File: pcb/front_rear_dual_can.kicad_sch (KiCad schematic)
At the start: 0 parts

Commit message: Configured hierarchical sheets and added CAN sheet.
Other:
- added sheet Cockpit (cockpit.kicad_sch)
- added sheet Front Zone (front_zone.kicad_sch)
- added sheet Power (power.kicad_sch)
- added sheet Rear Zone (rear_zone.kicad_sch)
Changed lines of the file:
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@@
 	(generator_version "10.0")
 	(paper "A4")
+	(sheet
+		(at 123.19 80.01)
+		(size 43.18 43.18)
+		(exclude_from_sim no)
+		(in_bom yes)
+		(on_board yes)
+		(dnp no)
+		(fields_autoplaced yes)
+		(stroke
+			(width 0.1524)
+			(type solid)
+		)
+		(fill
+			(color 0 0 0 0)
+		)
+		(property "Sheetname" "Power"
+			(at 123.19 79.2984 0)
+			(show_name no)
+			(do_not_autoplace no)
+			(effects
+				(font
+					(size 1.27 1.27)
+				)
+				(justify left bottom)
+			)
+		)
+		(property "Sheetfile" "power.kicad_sch"
+			(at 123.19 123.7746 0)
+			(show_name no)
+			(do_not_autoplace no)
+			(effects
+				(font
+					(size 1.27 1.27)
+				)
+				(justify left top)
+			)
+		)
+		(instances
+			(project "front_rear_dual_can"
+				(path "/11f1b6cb-7ca3-4657-a79b-c672c999e35e"
+					(page "5")
+				)
+			)
+		)
+	)
+	(sheet
+		(at 120.65 29.21)
+		(size 24.13 12.7)
+		(exclude_from_sim no)
+		(in_bom yes)
+		(on_board yes)
+		(dnp no)
+		(fields_autoplaced yes)
+		(stroke
+			(width 0.1524)
+			(type solid)
+		)
+		(fill
+			(color 0 0 0 0)
+		)
+		(property "Sheetname" "Cockpit"
+			(at 120.65 28.4984 0)
+			(show_name no)
+			(do_not_autoplace no)
+			(effects
+				(font
+					(size 1.27 1.27)
+				)
+				(justify left bottom)
+			)
+		)
+		(property "Sheetfile" "cockpit.kicad_sch"
+			(at 120.65 42.4946 0)
+			(show_name no)
+			(do_not_autoplace no)
+			(effects
+				(font
+					(size 1.27 1.27)
+				)
+				(justify left top)
+			)
+		)
+		(instances
+			(project "front_rear_dual_can"
+				(path "/11f1b6cb-7ca3-4657-a79b-c672c999e35e"
+					(page "4")
+				)
+			)
+		)
+	)
+	(sheet
+		(at 187.96 91.44)
+		(size 35.56 35.56)
+		(exclude_from_sim no)
+		(in_bom yes)
+		(on_board yes)
+		(dnp no)
+		(fields_autoplaced yes)
+		(stroke
+			(width 0.1524)
+			(type solid)
+		)
+		(fill
+			(color 0 0 0 0)
+		)
+		(property "Sheetname" "Front Zone"
+			(at 187.96 90.7284 0)
+			(show_name no)
+			(do_not_autoplace no)
+			(effects
+				(font
+					(size 1.27 1.27)
+				)
+				(justify left bottom)
+			)
+		)
+		(property "Sheetfile" "front_zone.kicad_sch"
+			(at 187.96 127.5846 0)
+			(show_name no)
+			(do_not_autoplace no)
+			(effects
+				(font
+					(size 1.27 1.27)
+				)
+				(justify left top)
+			)
+		)
+		(instances
+			(project "front_rear_dual_can"
+				(path "/11f1b6cb-7ca3-4657-a79b-c672c999e35e"
+					(page "2")
+				)
+			)
+		)
+	)
+	(sheet
+		(at 107.95 166.37)
+		(size 30.48 17.78)
+		(exclude_from_sim no)
+		(in_bom yes)
+		(on_board yes)
+		(dnp no)
+		(fields_autoplaced yes)
+		(stroke
+			(width 0.1524)
+			(type solid)
+		)
+		(fill
+			(color 0 0 0 0)
+		)
+		(property "Sheetname" "Rear Zone"
+			(at 107.95 165.6584 0)
+			(show_name no)
+			(do_not_autoplace no)
+			(effects
+				(font
+					(size 1.27 1.27)
+				)
+				(justify left bottom)
+			)
+		)
+		(property "Sheetfile" "rear_zone.kicad_sch"
+			(at 107.95 184.7346 0)
+			(show_name no)
+			(do_not_autoplace no)
+			(effects
+				(font
+					(size 1.27 1.27)
+				)
+				(justify left top)
+			)
+		)
+		(instances
+			(project "front_rear_dual_can"
+				(path "/11f1b6cb-7ca3-4657-a79b-c672c999e35e"
+					(page "3")
+				)
+			)
+		)
+	)
 	(sheet_instances
 		(path "/"

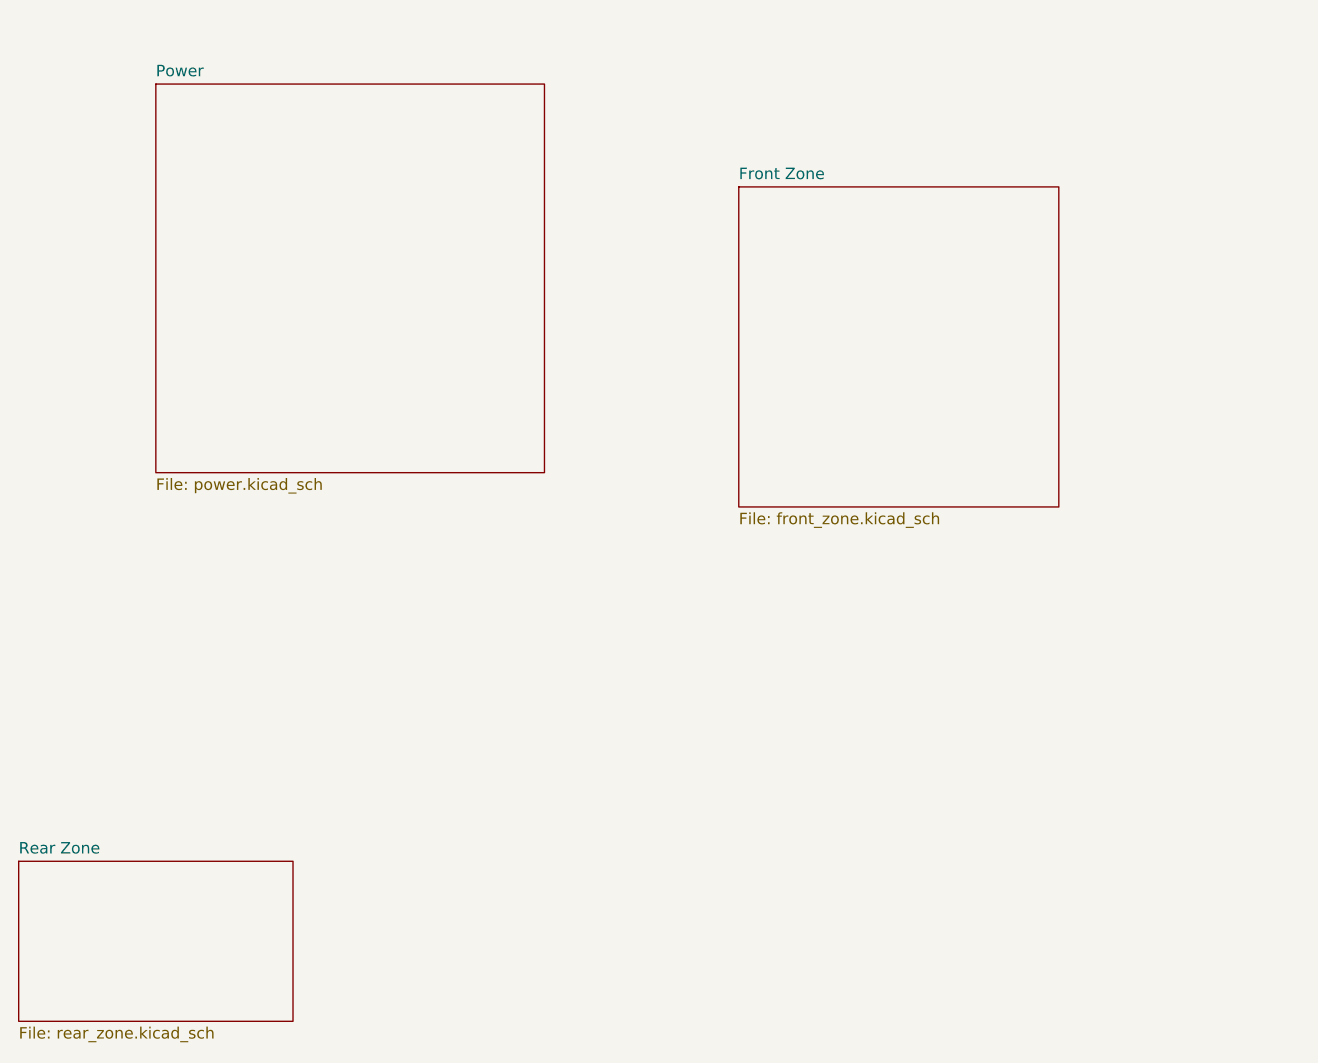
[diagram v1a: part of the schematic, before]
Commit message: Added Front and Rear zone sheets made of CAN and MCU design sheets.
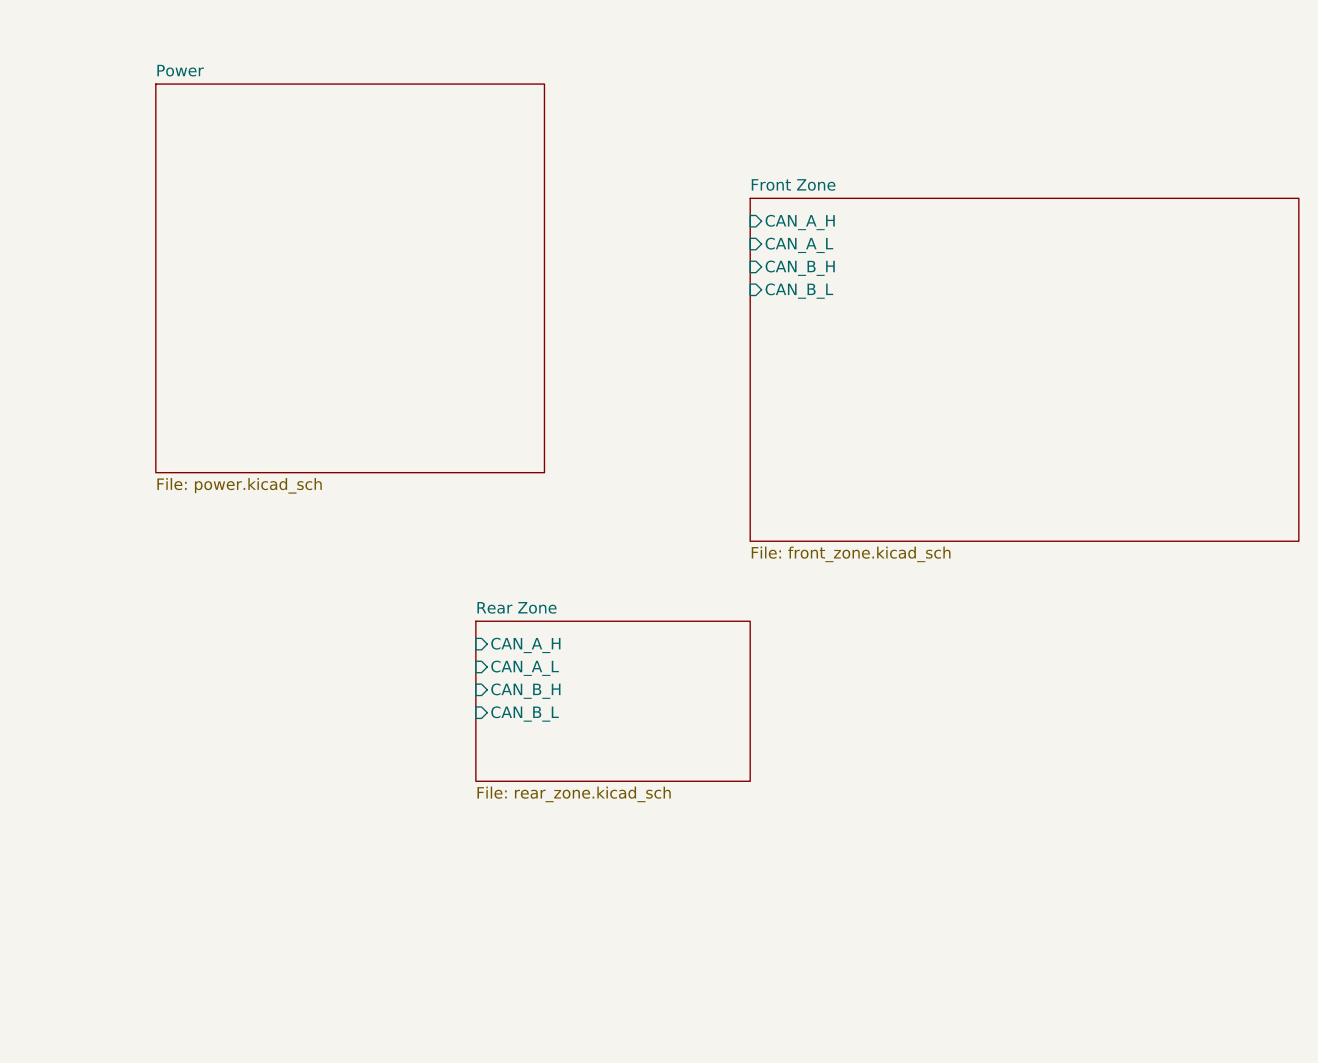
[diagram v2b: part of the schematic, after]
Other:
- sheet Front Zone ports: added CAN_A_H, CAN_A_L, CAN_B_H, CAN_B_L; removed none
- sheet Rear Zone ports: added CAN_A_H, CAN_A_L, CAN_B_H, CAN_B_L; removed none
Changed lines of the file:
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@@
 	)
 	(sheet
-		(at 187.96 91.44)
-		(size 35.56 35.56)
+		(at 189.23 92.71)
+		(size 60.96 38.1)
 		(exclude_from_sim no)
 		(in_bom yes)
@@
 		)
 		(property "Sheetname" "Front Zone"
-			(at 187.96 90.7284 0)
+			(at 189.23 91.9984 0)
 			(show_name no)
 			(do_not_autoplace no)
@@
 		)
 		(property "Sheetfile" "front_zone.kicad_sch"
-			(at 187.96 127.5846 0)
+			(at 189.23 131.3946 0)
 			(show_name no)
 			(do_not_autoplace no)
@@
 				)
 				(justify left top)
+			)
+		)
+		(pin "CAN_A_H" input
+			(at 189.23 95.25 180)
+			(effects
+				(font
+					(size 1.27 1.27)
+				)
+				(justify left)
+			)
+		)
+		(pin "CAN_A_L" input
+			(at 189.23 97.79 180)
+			(effects
+				(font
+					(size 1.27 1.27)
+				)
+				(justify left)
+			)
+		)
+		(pin "CAN_B_H" input
+			(at 189.23 100.33 180)
+			(effects
+				(font
+					(size 1.27 1.27)
+				)
+				(justify left)
+			)
+		)
+		(pin "CAN_B_L" input
+			(at 189.23 102.87 180)
+			(effects
+				(font
+					(size 1.27 1.27)
+				)
+				(justify left)
 			)
 		)
@@
 	)
 	(sheet
-		(at 107.95 166.37)
+		(at 158.75 139.7)
 		(size 30.48 17.78)
 		(exclude_from_sim no)
@@
 		)
 		(property "Sheetname" "Rear Zone"
-			(at 107.95 165.6584 0)
+			(at 158.75 138.9884 0)
 			(show_name no)
 			(do_not_autoplace no)
@@
 		)
 		(property "Sheetfile" "rear_zone.kicad_sch"
-			(at 107.95 184.7346 0)
+			(at 158.75 158.0646 0)
 			(show_name no)
 			(do_not_autoplace no)
@@
 			)
 		)
+		(pin "CAN_A_H" input
+			(at 158.75 142.24 180)
+			(effects
+				(font
+					(size 1.27 1.27)
+				)
+				(justify left)
+			)
+		)
+		(pin "CAN_A_L" input
+			(at 158.75 144.78 180)
+			(effects
+				(font
+					(size 1.27 1.27)
+				)
+				(justify left)
+			)
+		)
+		(pin "CAN_B_H" input
+			(at 158.75 147.32 180)
+			(effects
+				(font
+					(size 1.27 1.27)
+				)
+				(justify left)
+			)
+		)
+		(pin "CAN_B_L" input
+			(at 158.75 149.86 180)
+			(effects
+				(font
+					(size 1.27 1.27)
+				)
+				(justify left)
+			)
+		)

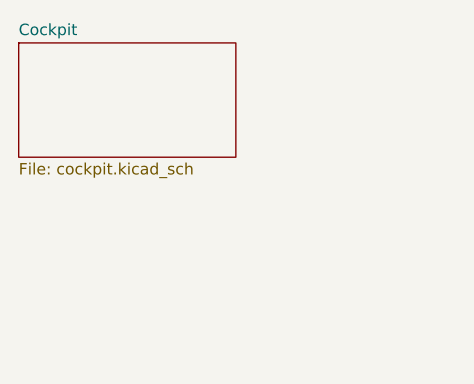
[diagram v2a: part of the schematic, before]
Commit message: Added Cockpit and Power sheets.
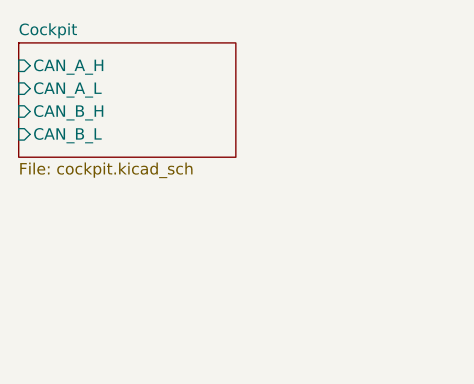
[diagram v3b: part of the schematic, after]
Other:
- sheet Cockpit ports: added CAN_A_H, CAN_A_L, CAN_B_H, CAN_B_L; removed none
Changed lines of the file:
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@@
+			)
+		)
+		(pin "CAN_A_H" input
+			(at 120.65 31.75 180)
+			(effects
+				(font
+					(size 1.27 1.27)
+				)
+				(justify left)
+			)
+		)
+		(pin "CAN_A_L" input
+			(at 120.65 34.29 180)
+			(effects
+				(font
+					(size 1.27 1.27)
+				)
+				(justify left)
+			)
+		)
+		(pin "CAN_B_H" input
+			(at 120.65 36.83 180)
+			(effects
+				(font
+					(size 1.27 1.27)
+				)
+				(justify left)
+			)
+		)
+		(pin "CAN_B_L" input
+			(at 120.65 39.37 180)
+			(effects
+				(font
+					(size 1.27 1.27)
+				)
+				(justify left)
 			)
 		)

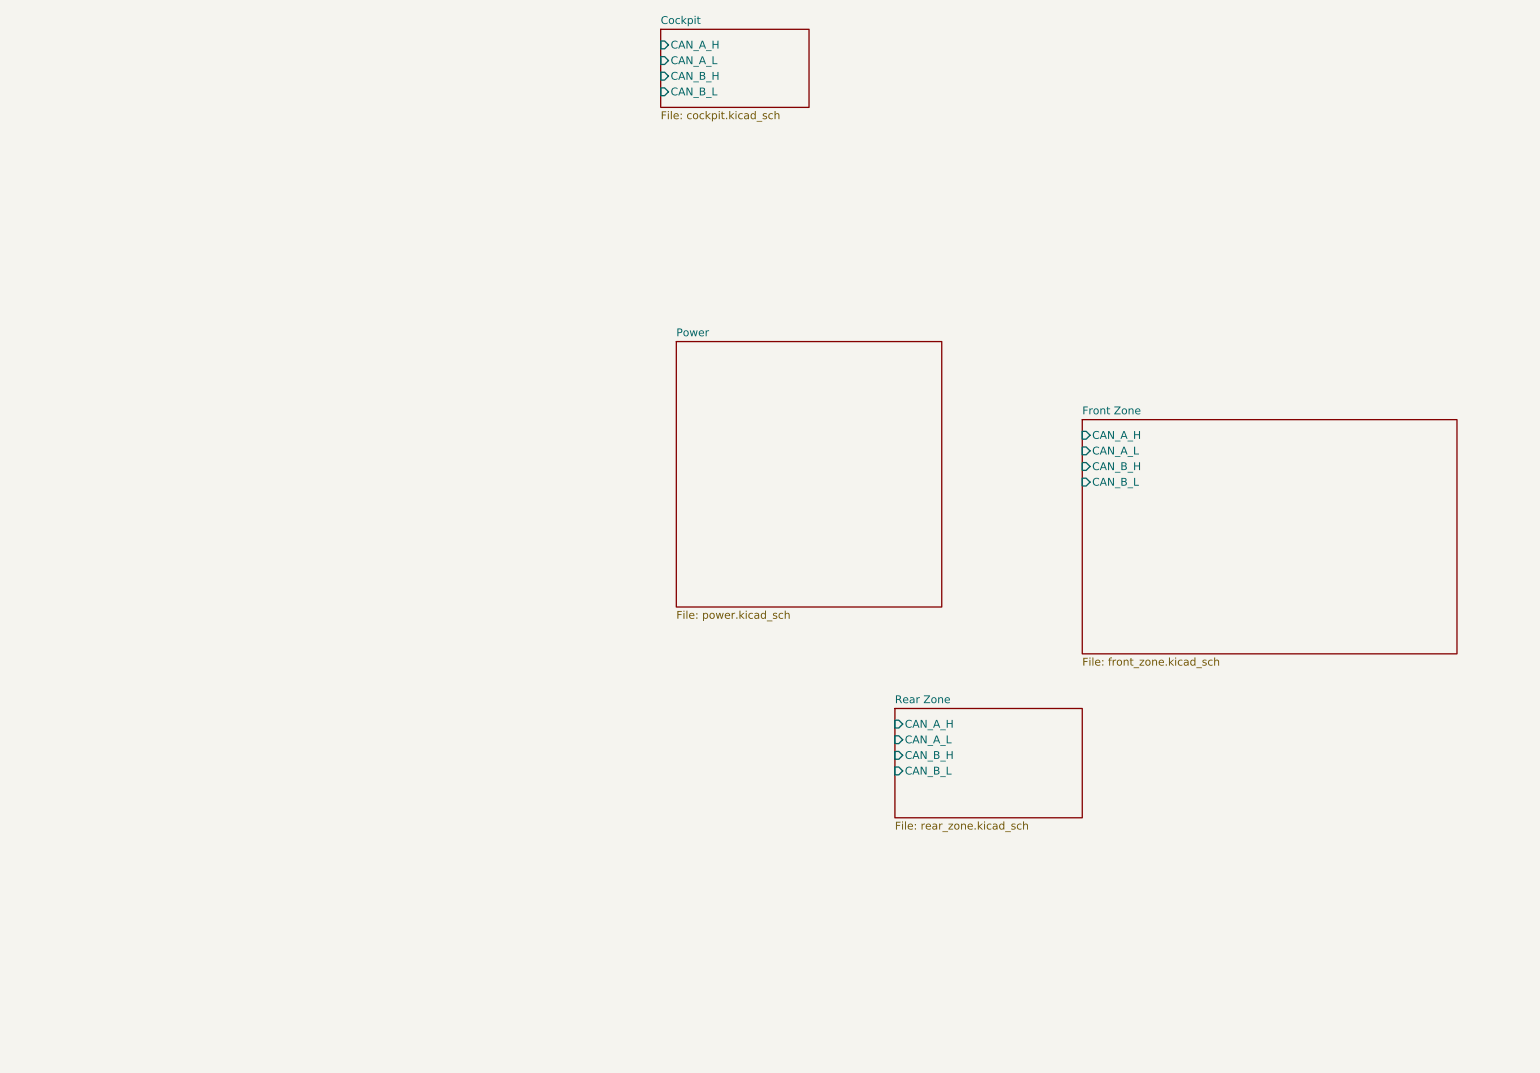
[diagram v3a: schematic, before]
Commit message: Added footprints to all components.
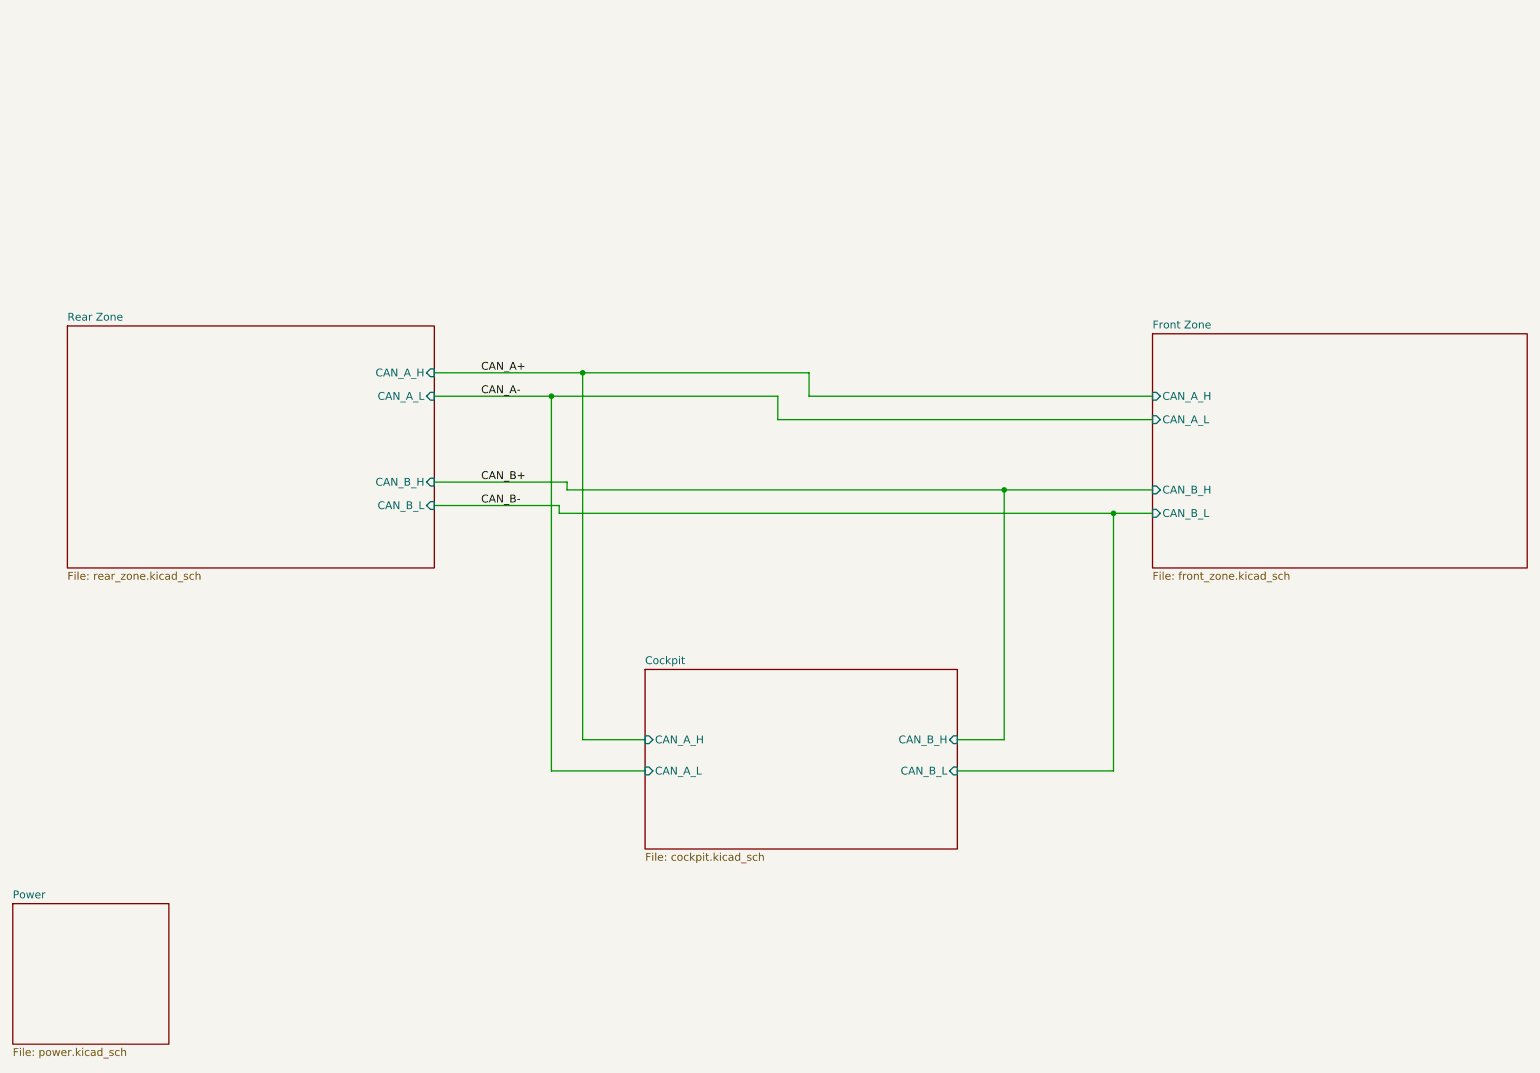
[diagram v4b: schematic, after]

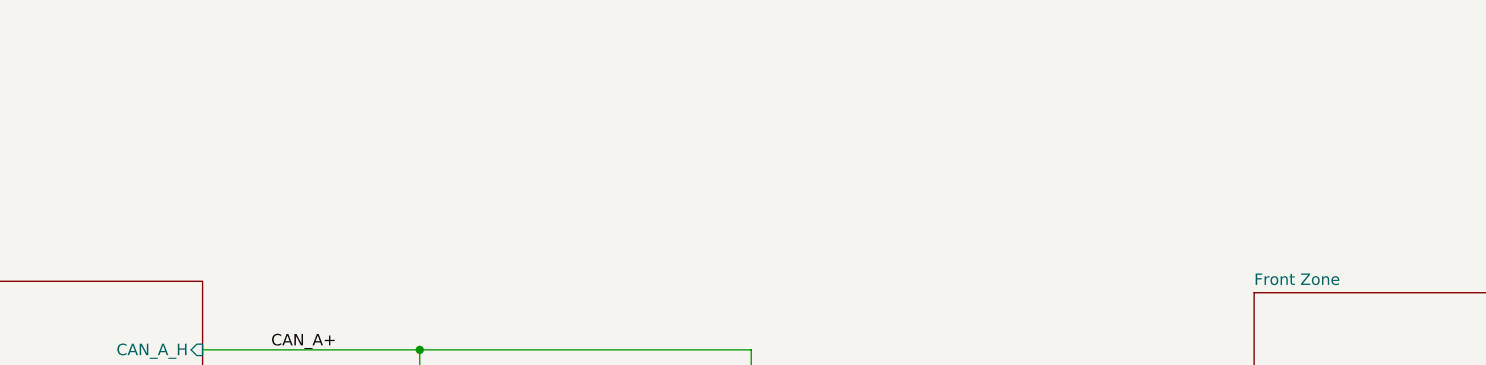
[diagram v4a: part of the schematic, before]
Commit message: Added CAN Bus connectors and finalized schematic with BOM, LCSC #s, and links to parts.
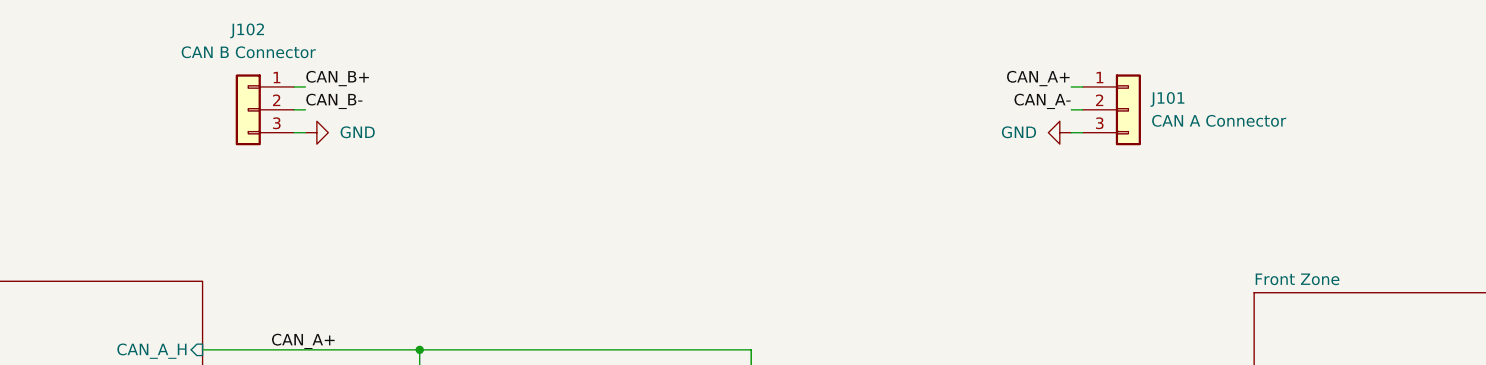
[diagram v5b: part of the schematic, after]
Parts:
- added J101: CAN A Connector, Connector_PinHeader_2.54mm:PinHeader_1x03_P2.54mm_Vertical, symbol Connector_Generic:Conn_01x03
- added J102: CAN B Connector, Connector_PinHeader_2.54mm:PinHeader_1x03_P2.54mm_Vertical, symbol Connector_Generic:Conn_01x03
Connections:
- net CAN_A+: now also J101.1 (Pin_1)
- net CAN_A-: now also J101.2 (Pin_2)
- net CAN_B+: now also J102.1 (Pin_1)
- net CAN_B-: now also J102.2 (Pin_2)
- new net GND: J101.3 (Pin_3), J102.3 (Pin_3)
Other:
- company: (none) -> 18-649 Lab 4: Controller PCB
- title: (none) -> Controller PCB: Top Level
